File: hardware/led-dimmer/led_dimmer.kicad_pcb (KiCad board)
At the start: 2 copper layers, 22 parts, among them J1 USB_B_Micro, Q1 Q_NMOS_GSD, Q2 Q_NMOS_GSD, SW1 Rotary_Encoder_Switch, U1 ATSAMD21G18A-AUT, U2 LD1117S33TR_SOT223

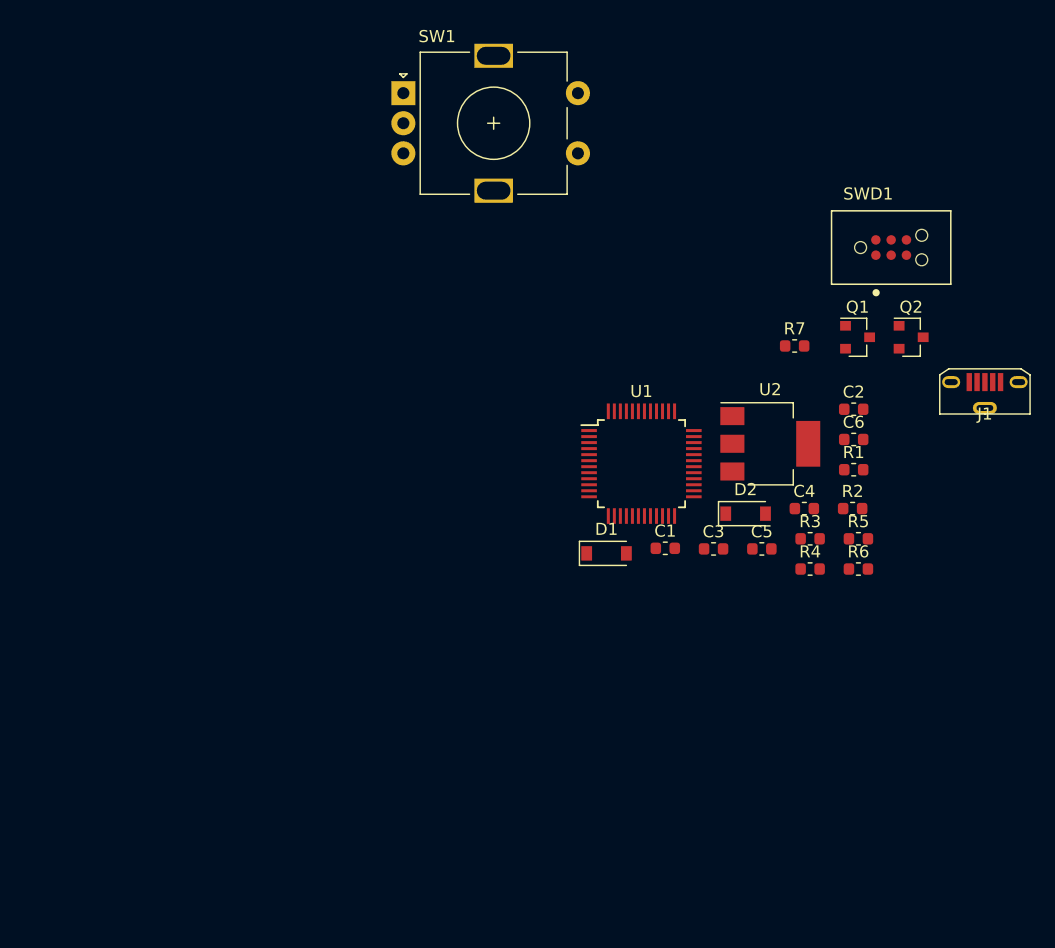
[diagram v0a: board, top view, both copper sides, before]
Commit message: Removed "unnecessary" components
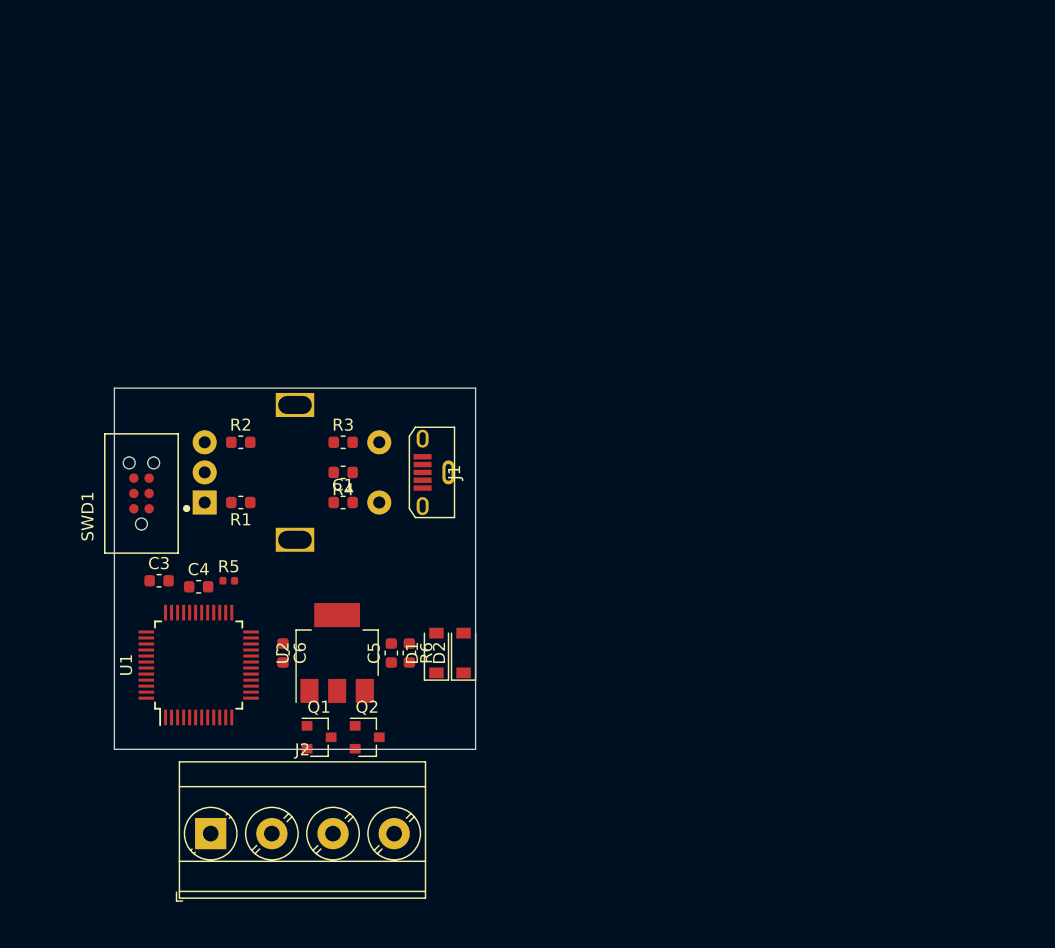
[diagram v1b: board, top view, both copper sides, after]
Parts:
- removed C2: C_Small, Capacitor_SMD:C_0603_1608Metric
- removed R7: 1k, Resistor_SMD:R_0603_1608Metric
- added J2: Screw_Terminal_01x04, TerminalBlock_Phoenix:TerminalBlock_Phoenix_MKDS-3-4-5.08_1x04_P5.08mm_Horizontal, F.Cu at (93.0, 122.0)
- R5: value R_Small -> Dummy; footprint Resistor_SMD:R_0603_1608Metric -> Resistor_SMD:R_0402_1005Metric
- SW1: moved to B.Cu
- moved SWD1 65.5 mm to (87.2, 93.8), turned to 90 degrees
- moved Q2 56.1 mm to (106.0, 114.0)
- moved Q1 55.7 mm to (102.0, 114.0)
- moved R5 52.4 mm to (94.5, 101.0)
- moved R2 51.1 mm to (95.5, 89.5)
- moved R1 51.0 mm to (95.5, 94.5), turned to 180 degrees
- moved C4 50.7 mm to (92.0, 101.5)
- moved C6 50.6 mm to (99.0, 107.0), turned to 270 degrees
- moved C3 46.1 mm to (88.7, 101.0)
- moved J1 44.9 mm to (112.8, 92.0), turned to 90 degrees
- moved U1 40.4 mm to (92.0, 108.0), turned to 90 degrees
- moved U2 40.0 mm to (103.5, 107.0), turned to 90 degrees
- moved R4 39.6 mm to (104.0, 92.0), turned to 180 degrees
- moved R3 39.6 mm to (104.0, 89.5)
- moved R6 37.9 mm to (109.5, 107.0), turned to 270 degrees
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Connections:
- net D4 renamed D4_PMOS_SWA
- net D9 renamed D9_PMOS_SWA
- R5 pad 1: Net-(R5-Pad1) -> GND
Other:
- board outline added: 30 x 30 mm

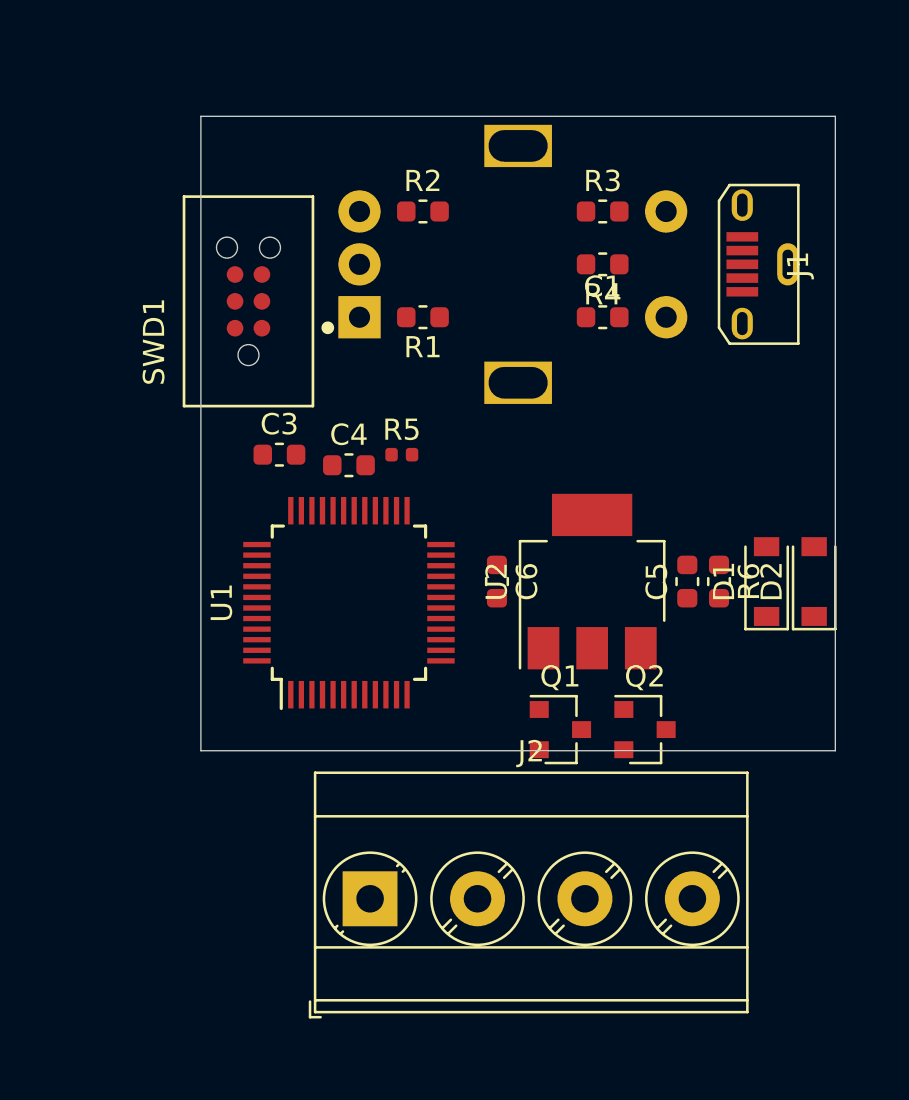
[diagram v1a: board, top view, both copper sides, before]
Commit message: Changed to just Pmosfet
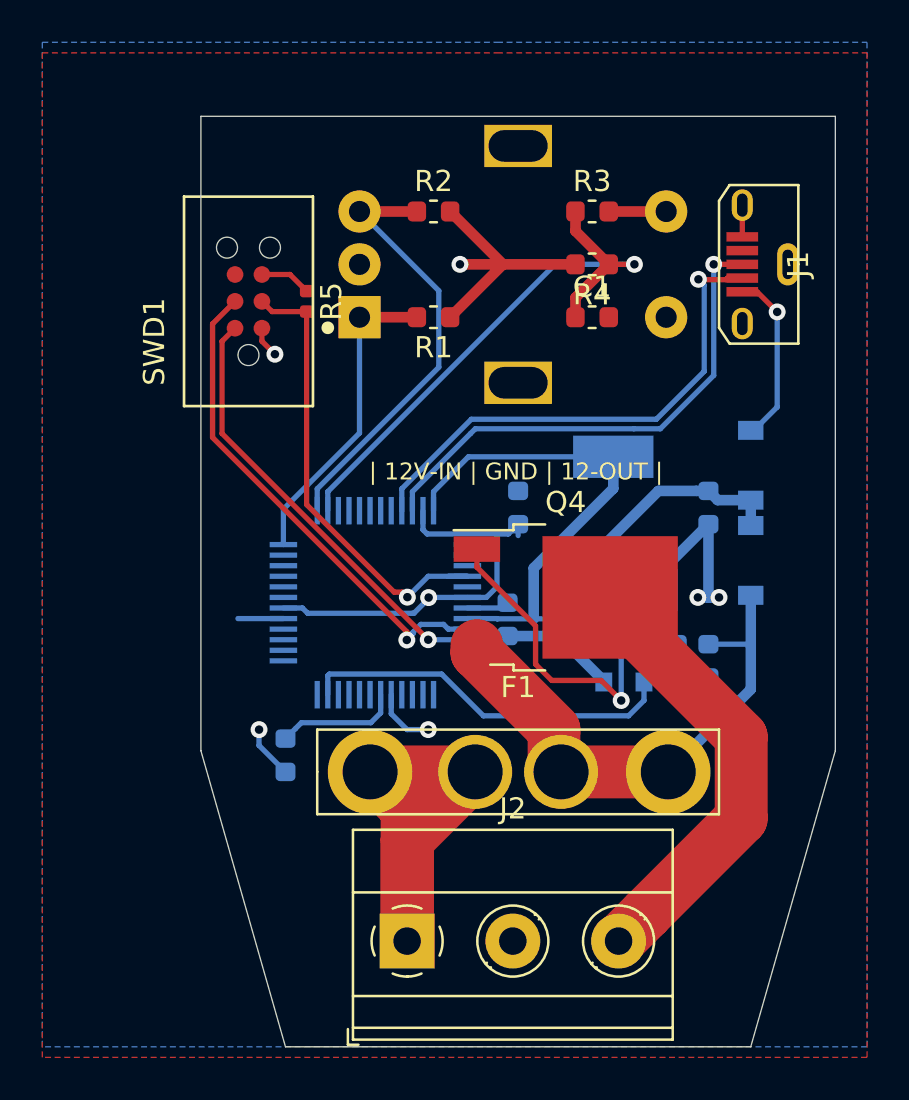
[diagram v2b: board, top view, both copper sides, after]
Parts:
- removed Q1, Q2: Q_NMOS_GSD, Package_TO_SOT_SMD:SOT-23
- removed R6: 1k, Resistor_SMD:R_0603_1608Metric
- added F1: Fuse_Small, Private Fuses:ATO_Fuseholder_3522-2, F.Cu at (100.0, 116.0)
- added Q3: Q_NMOS_GSD, Package_TO_SOT_SMD:SOT-23, B.Cu at (105.0, 110.8)
- added Q4: Q_PMOS_GDS, Package_TO_SOT_SMD:TO-252-2, F.Cu at (102.2, 107.8)
- added R7: 1k, Resistor_SMD:R_0603_1608Metric, B.Cu at (107.5, 110.8)
- added R8: 1k, Resistor_SMD:R_0603_1608Metric, B.Cu at (109.0, 110.8)
- C3, C4, C5, C6, D1, D2, U1, U2: moved to B.Cu
- J2: value Screw_Terminal_01x04 -> Screw_Terminal_01x03; footprint TerminalBlock_Phoenix:TerminalBlock_Phoenix_MKDS-3-4-5.08_1x04_P5.08mm_Horizontal -> TerminalBlock_Phoenix:TerminalBlock_Phoenix_MKDS-1,5-3_1x03_P5.00mm_Horizontal
- moved C3 14.2 mm to (89.0, 115.2), turned to 90 degrees
- moved C4 10.5 mm to (99.5, 108.8), turned to 90 degrees
- moved R5 8.53 mm to (90.0, 93.8), turned to 270 degrees
- moved D1 5.55 mm to (111.0, 101.5)
- moved C5 3.64 mm to (109.0, 103.5), turned to 270 degrees
- moved C6 3.64 mm to (100.0, 103.5)
- moved D2 3.16 mm to (111.0, 106.0), turned to 270 degrees
- moved U2 2.93 mm to (104.5, 104.2)
- moved J2 2.66 mm to (94.8, 124.0)
- moved U1 1.25 mm to (93.2, 108.0)
- moved C1 0.50 mm to (103.5, 94.5)
- moved R1 0.50 mm to (96.0, 94.5)
- moved R2 0.50 mm to (96.0, 89.5)
- moved R3 0.50 mm to (103.5, 89.5)
- moved R4 0.50 mm to (103.5, 92.0)
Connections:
- J2 pad 1: +12V -> Net-(F1-Pad2)
- J2 pad 3: SWA -> LED
- U1 pad 11: D8 -> D8_LED_POWER
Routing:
- net GND: track 0.00 -> 54.5 mm, vias 0 -> 5
- net +3V3: track 0.00 -> 49.0 mm, vias 0 -> 2
- net D13_ENC_SW: track 0.00 -> 27.4 mm, vias 0 -> 1
- net +12V: track 0.00 -> 24.7 mm
- net Net-(F1-Pad2): track 0.00 -> 24.6 mm
- net USB-: track 0.00 -> 24.2 mm, vias 0 -> 1
- net USB+: track 0.00 -> 24.0 mm, vias 0 -> 1
- net SWCLK: track 0.00 -> 23.6 mm, vias 0 -> 1
- net ~RESET: track 0.00 -> 22.2 mm, vias 0 -> 1
- net LED: track 0.00 -> 21.2 mm
- net SWDIO: track 0.00 -> 20.9 mm, vias 0 -> 1
- net D11_ENCB: track 0.00 -> 20.8 mm
- net D8_LED_POWER: track 0.00 -> 19.6 mm
- net Net-(Q3-Pad3): track 0.00 -> 19.1 mm, vias 0 -> 1
- net D5_ENCA: track 0.00 -> 15.0 mm
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- added copper zone on B.Cu, net +3V3
- added copper zone on F.Cu, net GND
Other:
- board size 30 x 30 mm -> 30 x 44 mm
- board text added: "| 12V-IN | GND | 12-OUT |"

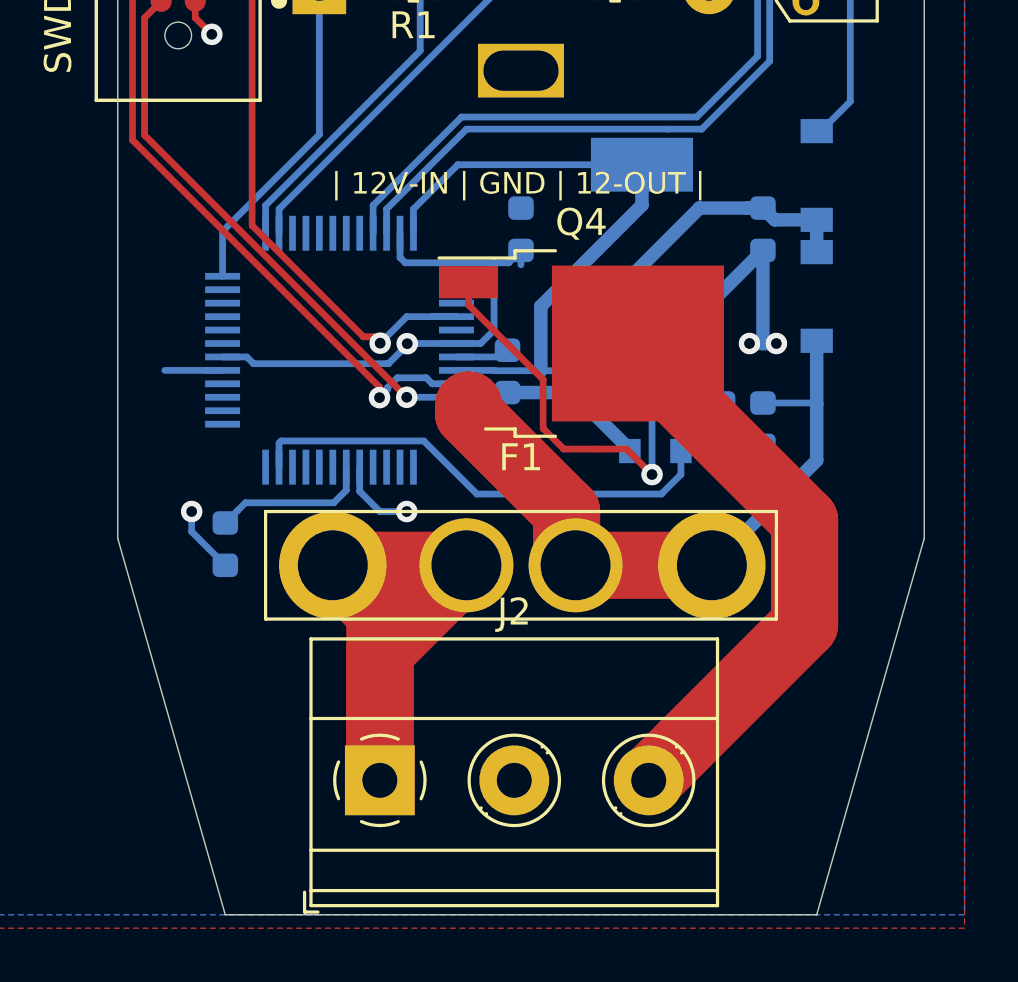
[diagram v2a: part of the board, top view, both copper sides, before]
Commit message: Changed to a 4-terminal block
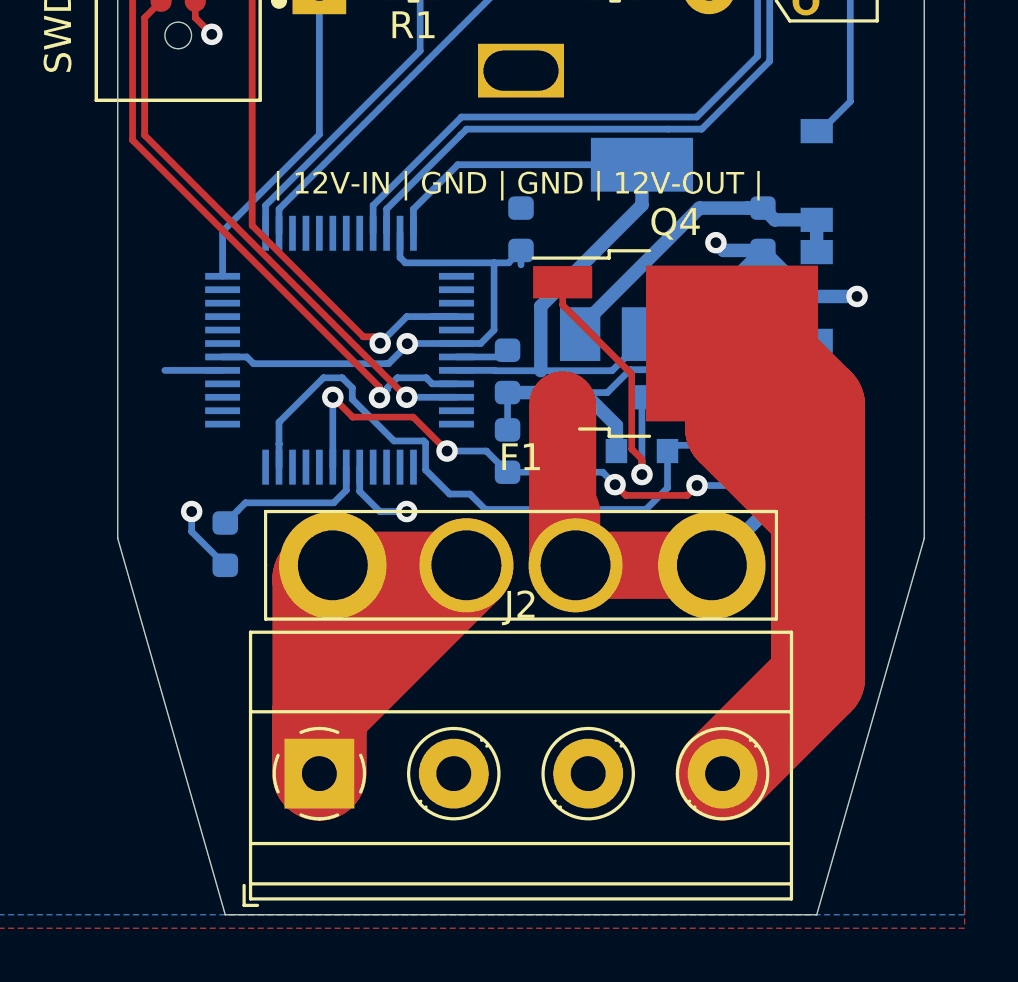
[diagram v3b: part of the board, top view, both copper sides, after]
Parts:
- added R6: 1k, Resistor_SMD:R_0603_1608Metric, B.Cu at (110.5, 110.8)
- added R9: 1k, Resistor_SMD:R_0603_1608Metric, B.Cu at (99.5, 111.8)
- F1: value Fuse_Small -> 5A
- J2: value Screw_Terminal_01x03 -> Screw_Terminal_01x04; footprint TerminalBlock_Phoenix:TerminalBlock_Phoenix_MKDS-1,5-3_1x03_P5.00mm_Horizontal -> TerminalBlock_Phoenix:TerminalBlock_Phoenix_MKDS-1,5-4_1x04_P5.00mm_Horizontal
- moved Q4 3.50 mm to (105.8, 107.8)
- moved J2 2.26 mm to (92.5, 123.8)
- moved Q3 0.50 mm to (104.5, 110.8)
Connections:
- J2 pad 3: LED -> GND
- U1 pad 7: A1 -> A1_BATVOLT
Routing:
- net A1_BATVOLT: track 0.00 -> 22.4 mm, vias 0 -> 4
- net LED: track 21.2 -> 27.0 mm
- net GND: track 54.5 -> 59.6 mm
- net +12V: track 24.7 -> 29.0 mm
- net D8_LED_POWER: track 19.6 -> 23.6 mm
- net Net-(Q3-Pad3): track 19.1 -> 16.5 mm
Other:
- board text added: "| 12V-IN | GND | GND | 12V-OUT |"
- board text removed: "| 12V-IN | GND | 12-OUT |"
